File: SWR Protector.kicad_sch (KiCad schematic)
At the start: 25 parts, among them J1 Barrel_Jack, J2 Barrel_Jack, J3 transceiver, J4 antenna, K2 ATX209, Q1 2N3904, T1 1:12, T2 12:1 ???, U1 LM78L05_TO92, U2 LM358

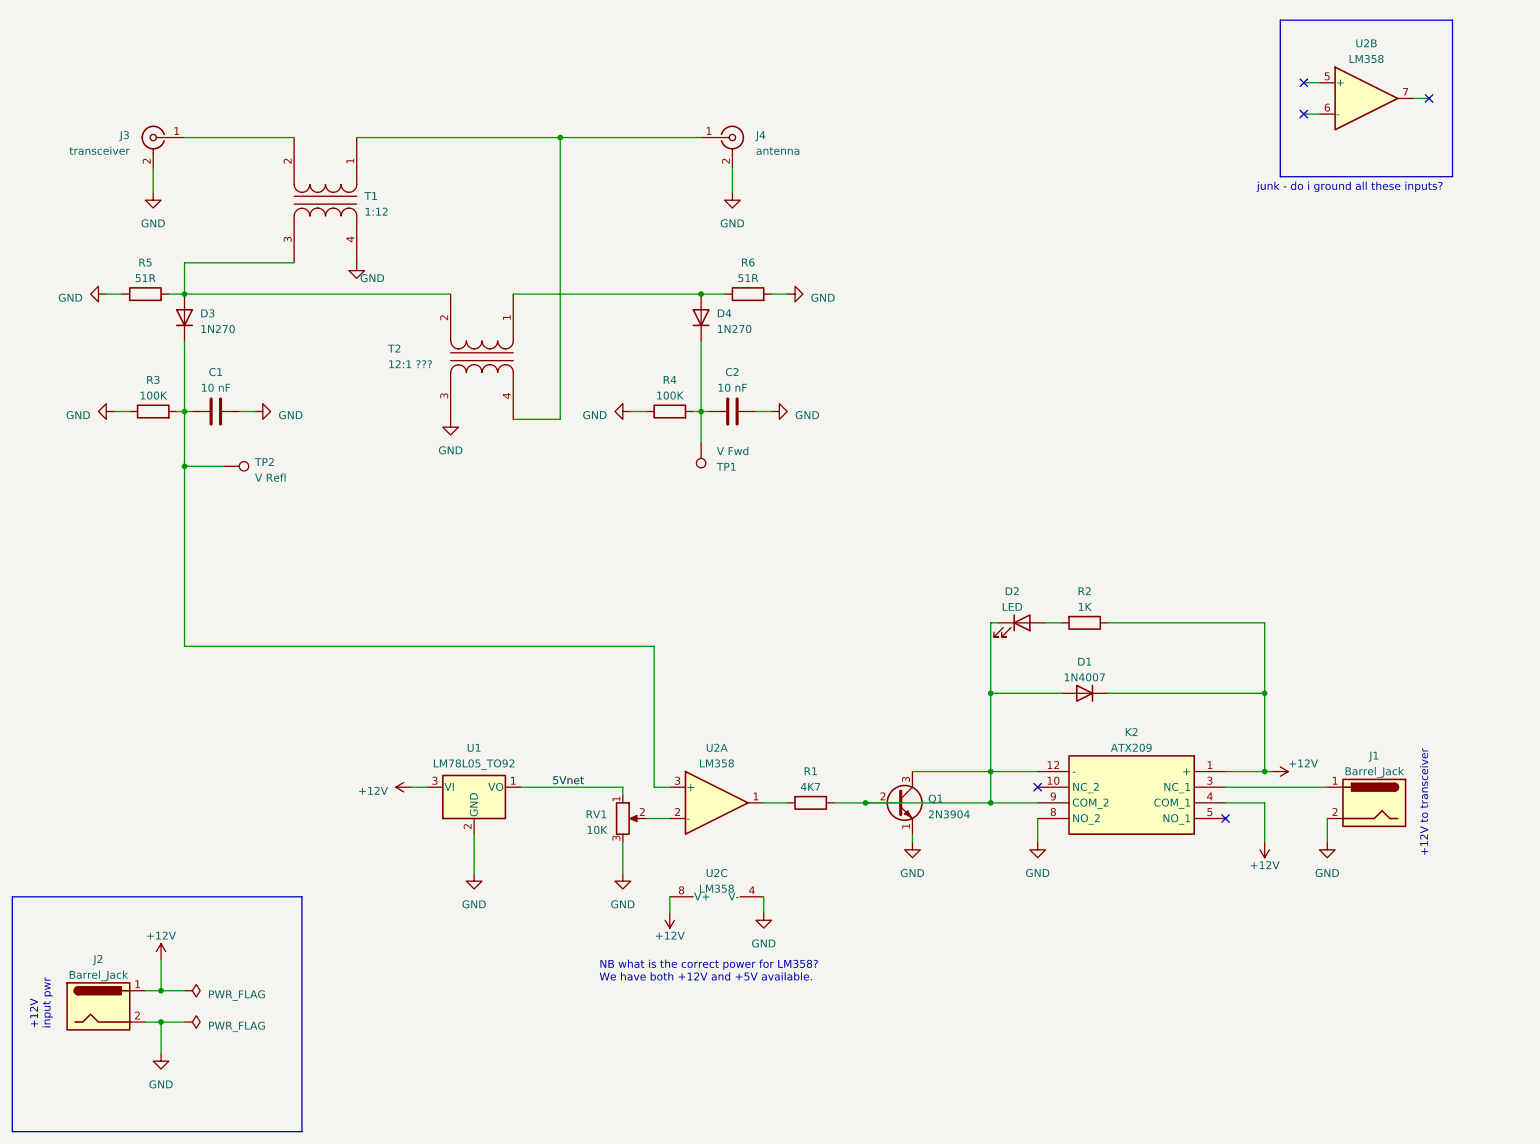
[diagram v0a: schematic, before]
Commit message: v0.4 swapped relay for Panasonic.  Much faster switching.  Reworked +5V ckt.
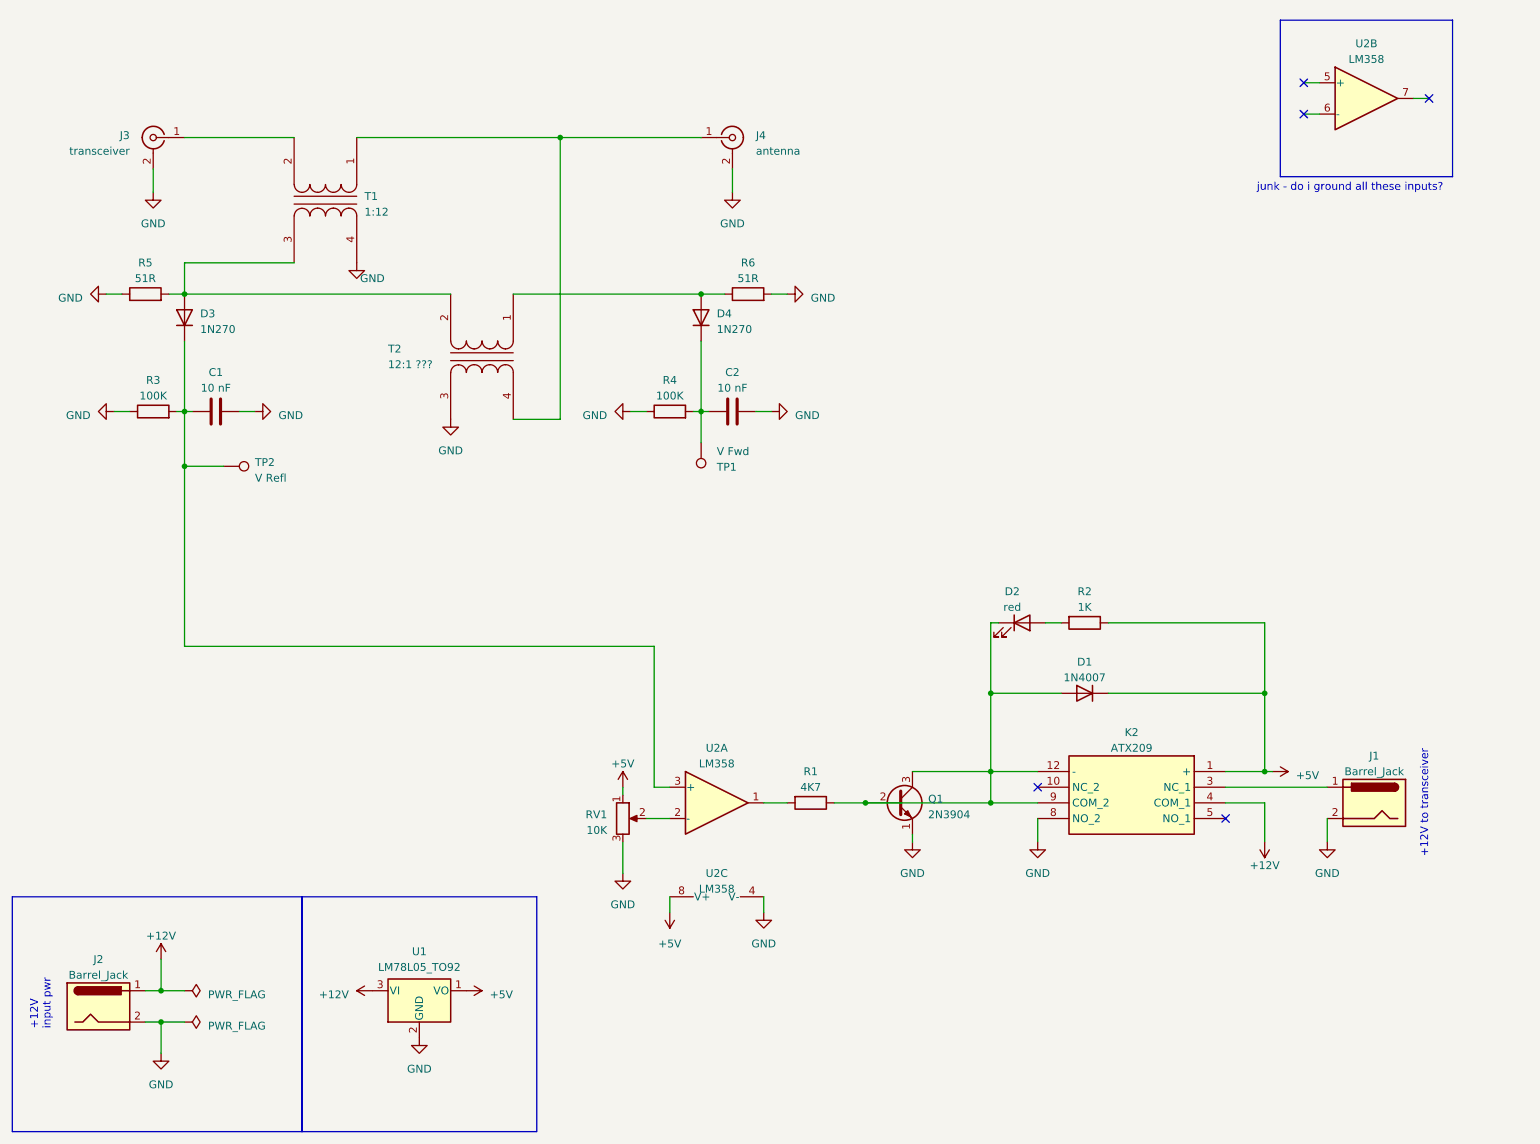
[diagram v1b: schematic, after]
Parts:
- D2: value LED -> red; footprint (none) -> LED_THT:LED_D5.0mm
- J1, J2: footprint (none) -> Connector_BarrelJack:BarrelJack_Horizontal
- T1, T2: footprint (none) -> Transformer_THT:Transformer_Toroid_Horizontal_D18.0mm
- TP1, TP2: footprint (none) -> TestPoint:TestPoint_THTPad_4.0x4.0mm_Drill2.0mm
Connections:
- net +12V: no longer D1.1 (K), K2.1 (+), R2.1, U2.8 (V+)
- net 5Vnet renamed +5V
- net +5V: now also D1.1 (K), K2.1 (+), R2.1, U2.8 (V+)
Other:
- note removed: "NB what is the correct power for LM358? We have both +12V and +5V available."
- moved on the sheet: U1

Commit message: 1. voltage divider in place 2. > Couple issues with the schematic... the base of Q1 is shown going    through the transistor to its own collector. That connection should    be removed.      Good eyes. That's an artifact of me moving groups of things around    on the page. Fixed. 3. > the 12v into the voltage regulator needs to come directly from the    12v input connector and NOT go through the relay contact.           I must be missing something.  I see +12V being generated off barrel    jack on left side (PWR_FLAG).  I *think* all the other +12V are common,    so the voltage regulator is getting that same +12V.  The relay has     +12V on COM_1, and the switched version of that is wired to the    second barrel jack.
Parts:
- added R7, R8: 10K, symbol Device:R
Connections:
- net +5V: now also R7.1
- net GND: now also R8.2
- net at D1.2 (A), D2.1 (K), K2.12 (-)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: no longer Q1.2 (B), R1.1
- net at U2.5 (+): now also R7.2, R8.1
- net at U2.6 (-): now also U2.7
- new net: Q1.2 (B), R1.1
- no-connect marks 5 -> 2
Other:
- note removed: "junk - do i ground all these inputs?"
- moved on the sheet: U2B
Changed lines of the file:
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@@
     (title "SWR Protector WA7GIL")
     (date "2023-05-06")
-    (rev "0.4")
+    (rev "0.5")
   )
   (junction (at 111.76 35.56) (diameter 0) (color 0 0 0 0)
@@
   (junction (at 134.62 80.01) (diameter 0) (color 0 0 0 0)
   )
-  (junction (at 161.29 143.51) (diameter 0) (color 0 0 0 0)
-  )
   (junction (at 134.62 60.96) (diameter 0) (color 0 0 0 0)
   )
-  (junction (at 181.61 143.51) (diameter 0) (color 0 0 0 0)
+  (junction (at 240.03 29.21) (diameter 0) (color 0 0 0 0)
   )
   (junction (at 46.99 179.07) (diameter 0) (color 0 0 0 0)
@@
   (junction (at 50.8 60.96) (diameter 0) (color 0 0 0 0)
   )
-  (no_connect (at 232.41 26.67))
-  (no_connect (at 232.41 31.75))
   (no_connect (at 189.23 140.97))
-  (no_connect (at 252.73 29.21))
   (no_connect (at 219.71 146.05))
+  (wire (pts (xy 242.57 34.29) (xy 242.57 39.37))
+    (stroke (width 0) (type default))
+  )
   (wire (pts (xy 46.99 184.15) (xy 46.99 179.07))
     (stroke (width 0) (type default))
@@
     (stroke (width 0) (type default))
   )
+  (wire (pts (xy 257.81 31.75) (xy 257.81 39.37))
+    (stroke (width 0) (type default))
+  )
   (wire (pts (xy 134.62 80.01) (xy 135.89 80.01))
     (stroke (width 0) (type default))
@@
     (stroke (width 0) (type default))
   )
-  (wire (pts (xy 232.41 31.75) (xy 234.95 31.75))
-    (stroke (width 0) (type default))
-  )
   (wire (pts (xy 182.88 114.3) (xy 181.61 114.3))
     (stroke (width 0) (type default))
@@
     (stroke (width 0) (type default))
   )
-  (wire (pts (xy 181.61 143.51) (xy 161.29 143.51))
-    (stroke (width 0) (type default))
-  )
   (wire (pts (xy 156.21 143.51) (xy 161.29 143.51))
     (stroke (width 0) (type default))
@@
     (stroke (width 0) (type default))
   )
-  (wire (pts (xy 232.41 26.67) (xy 234.95 26.67))
-    (stroke (width 0) (type default))
-  )
   (wire (pts (xy 50.8 88.9) (xy 50.8 118.11))
     (stroke (width 0) (type default))
@@
     (stroke (width 0) (type default))
   )
-  (wire (pts (xy 250.19 29.21) (xy 252.73 29.21))
-    (stroke (width 0) (type default))
-  )
   (wire (pts (xy 134.62 80.01) (xy 134.62 85.09))
     (stroke (width 0) (type default))
@@
     (stroke (width 0) (type default))
   )
+  (wire (pts (xy 257.81 39.37) (xy 242.57 39.37))
+    (stroke (width 0) (type default))
+  )
   (wire (pts (xy 127 140.97) (xy 129.54 140.97))
     (stroke (width 0) (type default))
@@
     (stroke (width 0) (type default))
   )
+  (wire (pts (xy 240.03 29.21) (xy 242.57 29.21))
+    (stroke (width 0) (type default))
+  )
   (wire (pts (xy 111.76 35.56) (xy 134.62 35.56))
     (stroke (width 0) (type default))
@@
     (fill (type none))
   )
-  (rectangle (start 228.6 16.51) (end 256.54 41.91)
+  (rectangle (start 232.41 15.24) (end 264.16 44.45)
     (stroke (width 0) (type default))
     (fill (type none))
@@
   )
   (text "+12V to transceiver" (at 252.73 152.4 90)
-    (effects (font (size 1.27 1.27)) (justify left bottom))
-  )
-  (text "junk - do i ground all these inputs?" (at 224.79 44.45 0)
     (effects (font (size 1.27 1.27)) (justify left bottom))
   )
@@
     )
   )
-  (symbol (lib_id "Amplifier_Operational:LM358") (at 242.57 29.21 0) (unit 2)
-    (in_bom yes) (on_board yes) (dnp no) (fields_autoplaced)
-    (property "Reference" "U2" (at 242.57 20.32 0)
-      (effects (font (size 1.27 1.27)))
-    )
-    (property "Value" "LM358" (at 242.57 22.86 0)
-      (effects (font (size 1.27 1.27)))
-    )
-    (property "Footprint" "" (at 242.57 29.21 0)
-      (effects (font (size 1.27 1.27)) hide)
-    )
-    (property "Datasheet" "http://www.ti.com/lit/ds/symlink/lm2904-n.pdf" (at 242.57 29.21 0)
+  (symbol (lib_id "Amplifier_Operational:LM358") (at 250.19 31.75 0) (unit 2)
+    (in_bom yes) (on_board yes) (dnp no) (fields_autoplaced)
+    (property "Reference" "U2" (at 250.19 22.86 0)
+      (effects (font (size 1.27 1.27)))
+    )
+    (property "Value" "LM358" (at 250.19 25.4 0)
+      (effects (font (size 1.27 1.27)))
+    )
+    (property "Footprint" "" (at 250.19 31.75 0)
+      (effects (font (size 1.27 1.27)) hide)
+    )
+    (property "Datasheet" "http://www.ti.com/lit/ds/symlink/lm2904-n.pdf" (at 250.19 31.75 0)
       (effects (font (size 1.27 1.27)) hide)
     )
@@
     )
   )
+  (symbol (lib_id "power:+5V") (at 240.03 21.59 0) (unit 1)
+    (in_bom yes) (on_board yes) (dnp no) (fields_autoplaced)
+    (property "Reference" "#PWR025" (at 240.03 25.4 0)
+      (effects (font (size 1.27 1.27)) hide)
+    )
+    (property "Value" "+5V" (at 240.03 17.78 0)
+      (effects (font (size 1.27 1.27)))
+    )
+    (property "Footprint" "" (at 240.03 21.59 0)
+      (effects (font (size 1.27 1.27)) hide)
+    )
+    (property "Datasheet" "" (at 240.03 21.59 0)
+      (effects (font (size 1.27 1.27)) hide)
+    )
+    (pin "1")
+    (instances
+      (project "SWR Protector"
+        (path "/46027dd5-036f-43c6-98e1-c4cfe473ecd7"
+          (reference "#PWR025") (unit 1)
+        )
+      )
+    )
+  )
   (symbol (lib_id "power:GND") (at 78.74 55.88 0) (unit 1)
     (in_bom yes) (on_board yes) (dnp no)
@@
         (path "/46027dd5-036f-43c6-98e1-c4cfe473ecd7"
           (reference "#PWR017") (unit 1)
+        )
+      )
+    )
+  )
+  (symbol (lib_id "Device:R") (at 240.03 33.02 0) (mirror y) (unit 1)
+    (in_bom yes) (on_board yes) (dnp no)
+    (property "Reference" "R8" (at 237.49 32.385 0)
+      (effects (font (size 1.27 1.27)) (justify left))
+    )
+    (property "Value" "10K" (at 237.49 34.925 0)
+      (effects (font (size 1.27 1.27)) (justify left))
+    )
+    (property "Footprint" "" (at 241.808 33.02 90)
+      (effects (font (size 1.27 1.27)) hide)
+    )
+    (property "Datasheet" "~" (at 240.03 33.02 0)
+      (effects (font (size 1.27 1.27)) hide)
+    )
+    (pin "1")
+    (pin "2")
+    (instances
+      (project "SWR Protector"
+        (path "/46027dd5-036f-43c6-98e1-c4cfe473ecd7"
+          (reference "R8") (unit 1)
         )
       )
@@
     )
   )
+  (symbol (lib_id "Device:R") (at 240.03 25.4 0) (mirror y) (unit 1)
+    (in_bom yes) (on_board yes) (dnp no)
+    (property "Reference" "R7" (at 237.49 24.765 0)
+      (effects (font (size 1.27 1.27)) (justify left))
+    )
+    (property "Value" "10K" (at 237.49 27.305 0)
+      (effects (font (size 1.27 1.27)) (justify left))
+    )
+    (property "Footprint" "" (at 241.808 25.4 90)
+      (effects (font (size 1.27 1.27)) hide)
+    )
+    (property "Datasheet" "~" (at 240.03 25.4 0)
+      (effects (font (size 1.27 1.27)) hide)
+    )
+    (pin "1")
+    (pin "2")
+    (instances
+      (project "SWR Protector"
+        (path "/46027dd5-036f-43c6-98e1-c4cfe473ecd7"
+          (reference "R7") (unit 1)
+        )
+      )
+    )
+  )
   (symbol (lib_id "power:GND") (at 39.37 80.01 270) (unit 1)
     (in_bom yes) (on_board yes) (dnp no) (fields_autoplaced)
@@
         )
       )
+    )
+  )
+  (symbol (lib_id "power:GND") (at 240.03 36.83 0) (unit 1)
+    (in_bom yes) (on_board yes) (dnp no) (fields_autoplaced)
+    (property "Reference" "#PWR026" (at 240.03 43.18 0)
+      (effects (font (size 1.27 1.27)) hide)
+    )
+    (property "Value" "GND" (at 240.03 41.91 0)
+      (effects (font (size 1.27 1.27)))
+    )
+    (property "Footprint" "" (at 240.03 36.83 0)
+      (effects (font (size 1.27 1.27)) hide)
+    )
+    (property "Datasheet" "" (at 240.03 36.83 0)
+      (effects (font (size 1.27 1.27)) hide)
+    )
+    (pin "1")
+    (instances
+      (project "SWR Protector"
+        (path "/46027dd5-036f-43c6-98e1-c4cfe473ecd7"
+          (reference "#PWR026") (unit 1)
+        )
+      )

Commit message: added notes for myself, started PCB layout and updated gitignore to ignore some Mac crap
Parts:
- C1, C2: footprint (none) -> Capacitor_THT:C_Disc_D5.0mm_W2.5mm_P5.00mm
- D3, D4: footprint (none) -> Diode_THT:D_DO-41_SOD81_P10.16mm_Horizontal
- J3, J4: footprint (none) -> Connector_Coaxial:BNC_TEConnectivity_1478035_Horizontal
- K2: footprint ATX209 -> KiCad:ATX209
- R1, R2, R3, R4, R5, R6, R7, R8, RV1: footprint (none) -> Resistor_THT:R_Axial_DIN0207_L6.3mm_D2.5mm_P7.62mm_Horizontal
- U2: footprint (none) -> KiCAD:LM358
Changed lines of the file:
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@@
       (effects (font (size 1.27 1.27)))
     )
-    (property "Footprint" "" (at 143.51 79.0448 0)
+    (property "Footprint" "Capacitor_THT:C_Disc_D5.0mm_W2.5mm_P5.00mm" (at 143.51 79.0448 0)
       (effects (font (size 1.27 1.27)) hide)
     )
@@
       (effects (font (size 1.27 1.27)))
     )
-    (property "Footprint" "" (at 152.4 141.732 90)
+    (property "Footprint" "Resistor_THT:R_Axial_DIN0207_L6.3mm_D2.5mm_P7.62mm_Horizontal" (at 152.4 141.732 90)
       (effects (font (size 1.27 1.27)) hide)
     )
@@
       (effects (font (size 1.27 1.27)))
     )
-    (property "Footprint" "" (at 44.45 62.738 90)
+    (property "Footprint" "Resistor_THT:R_Axial_DIN0207_L6.3mm_D2.5mm_P7.62mm_Horizontal" (at 44.45 62.738 90)
       (effects (font (size 1.27 1.27)) hide)
     )
@@
       (effects (font (size 1.27 1.27)))
     )
-    (property "Footprint" "" (at 59.69 79.0448 0)
+    (property "Footprint" "Capacitor_THT:C_Disc_D5.0mm_W2.5mm_P5.00mm" (at 59.69 79.0448 0)
       (effects (font (size 1.27 1.27)) hide)
     )
@@
       (effects (font (size 1.27 1.27)) (justify right))
     )
-    (property "Footprint" "" (at 50.8 64.77 0)
+    (property "Footprint" "Diode_THT:D_DO-41_SOD81_P10.16mm_Horizontal" (at 50.8 64.77 0)
       (effects (font (size 1.27 1.27)) hide)
     )
@@
       (effects (font (size 1.27 1.27)) (justify right))
     )
-    (property "Footprint" "" (at 134.62 64.77 0)
+    (property "Footprint" "Diode_THT:D_DO-41_SOD81_P10.16mm_Horizontal" (at 134.62 64.77 0)
       (effects (font (size 1.27 1.27)) hide)
     )
@@
       (effects (font (size 1.27 1.27)) (justify left))
     )
-    (property "Footprint" "" (at 45.72 35.56 0)
+    (property "Footprint" "Connector_Coaxial:BNC_TEConnectivity_1478035_Horizontal" (at 45.72 35.56 0)
       (effects (font (size 1.27 1.27)) hide)
     )
@@
       (effects (font (size 1.27 1.27)))
     )
-    (property "Footprint" "" (at 250.19 31.75 0)
+    (property "Footprint" "KiCAD:LM358" (at 250.19 31.75 0)
       (effects (font (size 1.27 1.27)) hide)
     )
@@
       (effects (font (size 1.27 1.27)) (justify right))
     )
-    (property "Footprint" "" (at 121.92 146.05 0)
+    (property "Footprint" "Resistor_THT:R_Axial_DIN0207_L6.3mm_D2.5mm_P7.62mm_Horizontal" (at 121.92 146.05 0)
       (effects (font (size 1.27 1.27)) hide)
     )
@@
       (effects (font (size 1.27 1.27)))
     )
-    (property "Footprint" "" (at 142.24 62.738 90)
+    (property "Footprint" "Resistor_THT:R_Axial_DIN0207_L6.3mm_D2.5mm_P7.62mm_Horizontal" (at 142.24 62.738 90)
       (effects (font (size 1.27 1.27)) hide)
     )
@@
       (effects (font (size 1.27 1.27)))
     )
-    (property "Footprint" "" (at 45.72 81.788 90)
+    (property "Footprint" "Resistor_THT:R_Axial_DIN0207_L6.3mm_D2.5mm_P7.62mm_Horizontal" (at 45.72 81.788 90)
       (effects (font (size 1.27 1.27)) hide)
     )
@@
       (effects (font (size 1.27 1.27)))
     )
-    (property "Footprint" "" (at 196.85 112.522 90)
+    (property "Footprint" "Resistor_THT:R_Axial_DIN0207_L6.3mm_D2.5mm_P7.62mm_Horizontal" (at 196.85 112.522 90)
       (effects (font (size 1.27 1.27)) hide)
     )
@@
       (effects (font (size 1.27 1.27)) (justify left))
     )
-    (property "Footprint" "" (at 241.808 33.02 90)
+    (property "Footprint" "Resistor_THT:R_Axial_DIN0207_L6.3mm_D2.5mm_P7.62mm_Horizontal" (at 241.808 33.02 90)
       (effects (font (size 1.27 1.27)) hide)
     )
@@
       (effects (font (size 1.27 1.27)) (justify left))
     )
-    (property "Footprint" "" (at 139.7 35.56 0)
+    (property "Footprint" "Connector_Coaxial:BNC_TEConnectivity_1478035_Horizontal" (at 139.7 35.56 0)
       (effects (font (size 1.27 1.27)) hide)
     )
@@
       (effects (font (size 1.27 1.27)))
     )
-    (property "Footprint" "ATX209" (at 193.04 233.35 0)
+    (property "Footprint" "KiCad:ATX209" (at 193.04 233.35 0)
       (effects (font (size 1.27 1.27)) (justify left top) hide)
     )
@@
       (effects (font (size 1.27 1.27)) (justify left))
     )
-    (property "Footprint" "" (at 241.808 25.4 90)
+    (property "Footprint" "Resistor_THT:R_Axial_DIN0207_L6.3mm_D2.5mm_P7.62mm_Horizontal" (at 241.808 25.4 90)
       (effects (font (size 1.27 1.27)) hide)
     )
@@
       (effects (font (size 1.27 1.27)))
     )
-    (property "Footprint" "" (at 137.16 161.29 0)
+    (property "Footprint" "KiCAD:LM358" (at 137.16 161.29 0)
       (effects (font (size 1.27 1.27)) hide)
     )
@@
       (effects (font (size 1.27 1.27)))
     )
-    (property "Footprint" "" (at 137.16 143.51 0)
+    (property "Footprint" "KiCAD:LM358" (at 137.16 143.51 0)
       (effects (font (size 1.27 1.27)) hide)
     )
@@
       (effects (font (size 1.27 1.27)))
     )
-    (property "Footprint" "" (at 129.54 81.788 90)
-      (effects (font (size 1.27 1.27)) hide)
-    )
+    (property "Footprint" "Resistor_THT:R_Axial_DIN0207_L6.3mm_D2.5mm_P7.62mm_Horizontal" (at 129.54 81.788 90)
+      (effects (font (size 1.27 1.27)) hide)
+    )
